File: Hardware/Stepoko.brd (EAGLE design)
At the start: 150 x 80 mm, 172 parts, among them J1 AVR ISP, Q1 16MHZ, Q2 100A/100V, U1 ATMEGA328, U2 CY7C65213, U3 74LVC1G04, U4 LM25011, U5 DRV8811, U6 74HC7014D, U7 74AHC1G08, U8 DRV8811, U9 DRV8811

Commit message: revision changes from review
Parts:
- added C43: 1000pF, SparkFun-Capacitors:0603-CAP
- moved C20 1.02 mm to (15.5, 40.5)
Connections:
- new net N$1: R54.1, U4.7
- net GND: no longer R54.1

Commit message: made changes from design review
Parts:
- removed SJ1: Limit Pull Direction, SparkFun-Passives:PAD-JUMPER-3-2OF3_NC_BY_TRACE_YES_SILK_LARGE
- removed U$3: (no value), SparkFun-Boards:FLANGED_RED_ENCLOSURE-OUTLINE
- added C45, C46: 0.1uF, SparkFun-Capacitors:0603-CAP
- added S5: DPDT, SparkFun-Electromechanical:AYZ0202
- added U$1: (no value), SparkFun-Boards:FLANGED_RED_ENCLOSURE-DIMENSION-NO-INNER-HOLES
- C43: value 1000pF -> 0.1uF
- S1, S2, S3: value 2-POS-DIP -> 2-POS-DIPCTS-THRU-HOLE; device SparkFun-Electromechanical:CHS-02A -> SparkFun-Electromechanical:209-2LPST
- moved S3 1.14 mm to (54.0, 48.0)
- moved C11 1.02 mm to (40.0, 40.5)
- moved C31 1.02 mm to (64.5, 40.5)
- moved S1 0.92 mm to (4.99, 47.8)
- moved S2 0.80 mm to (29.7, 47.8)
- moved LOGO2 0.80 mm to (64.0, 8.89)
- moved D17 0.51 mm to (122.0, 77.3)
- moved R54 0.51 mm to (123.3, 74.6)
- turned C43 to 180 degrees
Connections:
- new net N$4: JP1.1, JP3.1, JP4.1, S5.5
- net 5V: now also S5.1, S5.6; no longer R40.2, SJ1.3
- net ESTOP: now also R40.2; no longer D7.C
- net GND: now also C43.2, C45.2, C46.2, D7.C, S5.3, S5.4; no longer JP1.1, JP3.1, JP4.1, SJ1.1
- net N$95: now also S5.2; no longer SJ1.2
- net VIN: now also C43.1, C45.1, C46.1
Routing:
- net N$4: track 0.00 -> 47.7 mm, vias 0 -> 1
- net 5V: track 521.0 -> 532.5 mm, vias 33 -> 32
- net ESTOP: track 97.2 -> 90.0 mm
- net N$95: track 35.6 -> 42.6 mm
- net N$1: track 0.00 -> 4.19 mm
- net GND: track 0.00 -> 3.39 mm, vias 119 -> 123
- net N$15: track 21.3 -> 20.7 mm, vias 2 -> 1
- net N$34: track 21.3 -> 20.8 mm, vias 2 -> 1
- net N$77: track 22.8 -> 23.3 mm, vias 2 -> 1
- net N$76: track 21.3 -> 21.1 mm, vias 2 -> 1
- net N$35: track 22.8 -> 23.0 mm, vias 2 -> 1
- net N$23: track 22.8 -> 22.9 mm, vias 2 -> 1
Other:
- board text added: "Limit Switch"
- board text added: "Pull Down"
- board text added: "Pull Up"
- board text removed: "Limit"
- board text removed: "Switch Pull +5v-UP GND-DOWN"

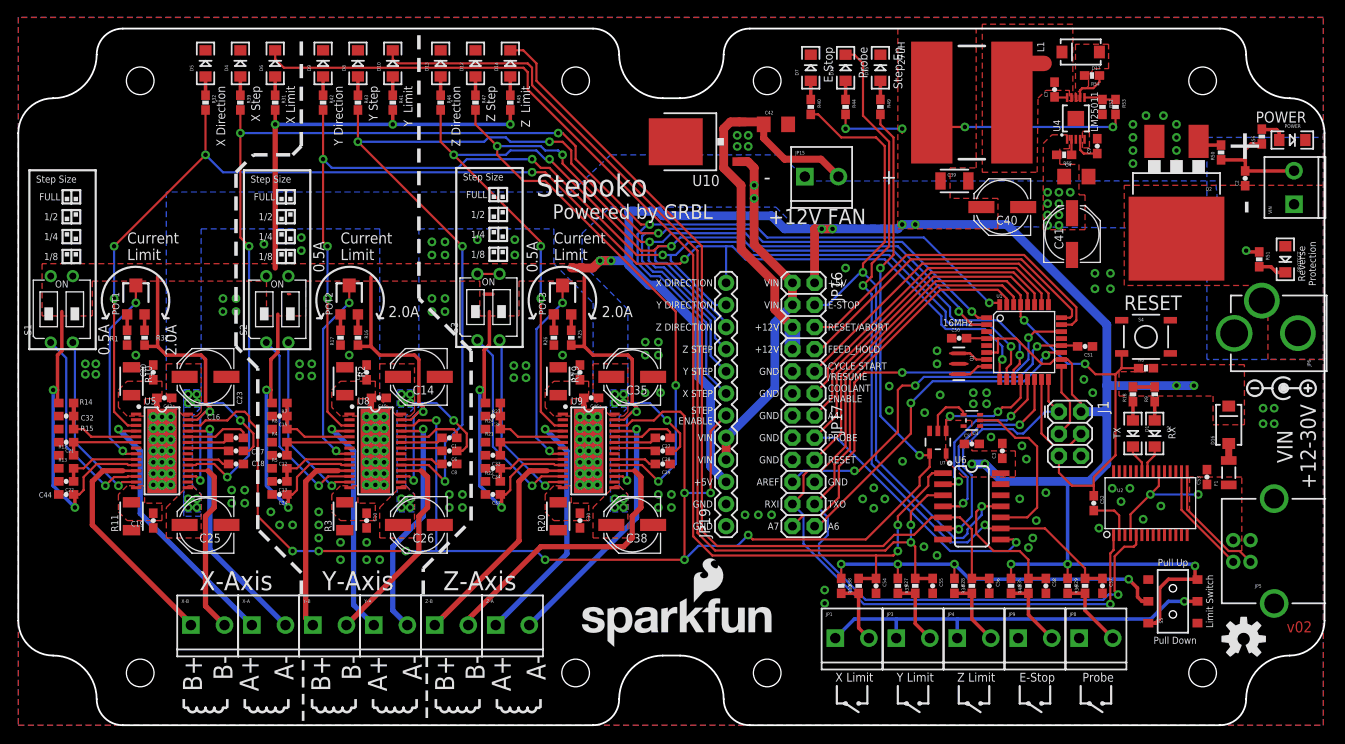
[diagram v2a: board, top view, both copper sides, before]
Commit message: added prod-ids
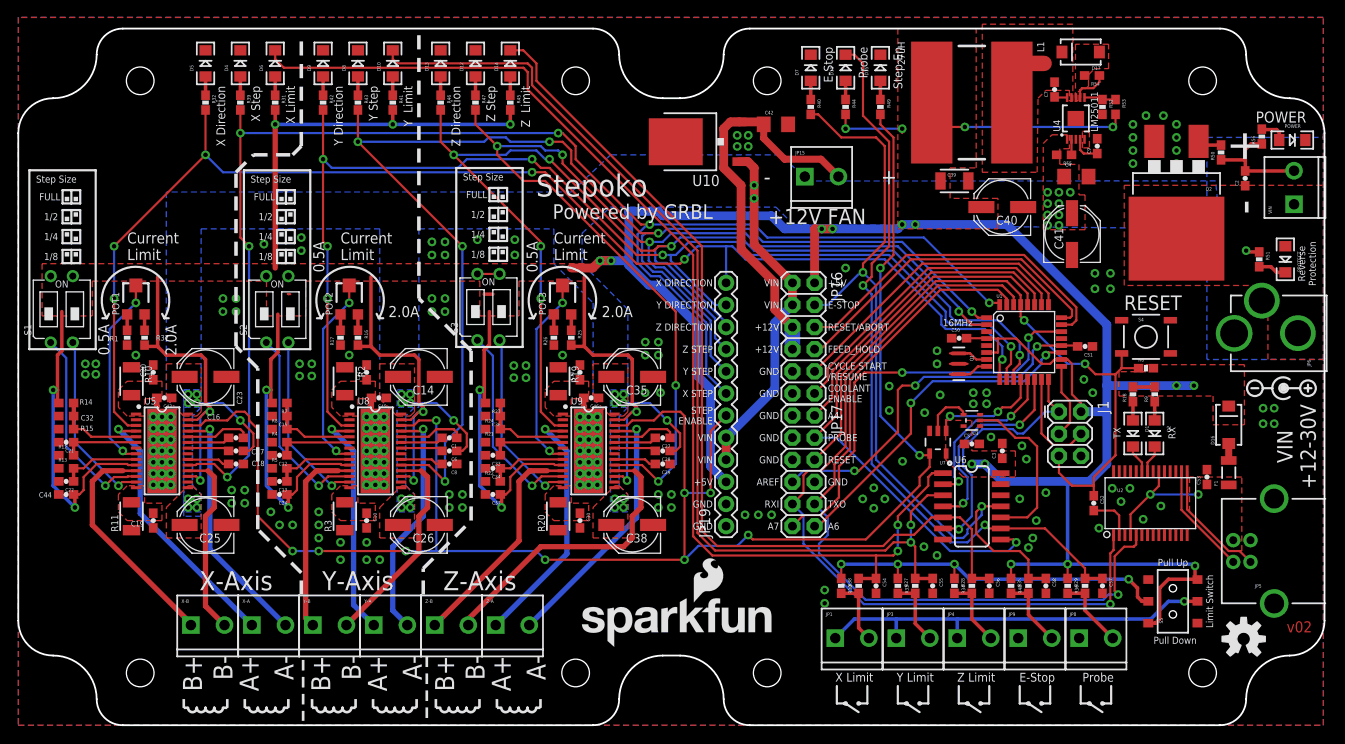
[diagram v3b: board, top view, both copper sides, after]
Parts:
- C15, C32, C36: device SparkFun:0603-CAP -> SparkFun-Capacitors:0603
- R53, R54, R55: device SparkFun-Passives:0603-RES -> SparkFun-Resistors:0603
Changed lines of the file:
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@@
 <attribute name="PROD_ID" value="CAP-10547" x="21.5" y="40" size="1.778" layer="27" rot="R180" display="off"/>
 </element>
-<element name="C32" library="SparkFun" package="0603-CAP" value="0.18uF" x="5.5" y="35.5" smashed="yes" rot="R180">
+<element name="C32" library="SparkFun-Capacitors" package="0603" value="0.18uF" x="5.5" y="35.5" smashed="yes" rot="R180">
 <attribute name="NAME" x="7.1782" y="34.9938" size="0.6096" layer="25" font="vector"/>
 <attribute name="VALUE" x="7.278" y="36.389" size="0.4064" layer="27" font="vector" rot="R270"/>
+<attribute name="PROD_ID" value="CAP-12380" x="5.5" y="35.5" size="1.778" layer="27" rot="R180" display="off"/>
 </element>
 <element name="R37" library="SparkFun-Resistors" package="0603-RES" value="1K" x="14.5" y="44.5" smashed="yes" rot="R270">
@@
 <attribute name="PROD_ID" value="IC-12375" x="16.5" y="31.5" size="1.778" layer="27" rot="R270" display="off"/>
 </element>
-<element name="S1" library="SparkFun-Electromechanical" package="209-2LPST" value="2-POS-DIPCTS-THRU-HOLE" x="4.992" y="47.762"/>
+<element name="S1" library="SparkFun-Electromechanical" package="209-2LPST" value="2-POS-DIPCTS-THRU-HOLE" x="4.992" y="47.762">
+<attribute name="PROD_ID" value="SWCH-12532" x="4.992" y="47.762" size="1.778" layer="27" display="off"/>
+</element>
 <element name="C25" library="SparkFun-Capacitors" package="PANASONIC_D" value="47uF" x="21.5" y="23" rot="R180">
 <attribute name="PROD_ID" value="CAP-10547" x="21.5" y="23" size="1.016" layer="27" font="vector" ratio="15" rot="R180" display="off"/>
@@
 <attribute name="PROD_ID" value="CAP-10547" x="63" y="75" size="1.778" layer="27" rot="R180" display="off"/>
 </element>
-<element name="C15" library="SparkFun" package="0603-CAP" value="0.18uF" x="30" y="35.5" rot="R180"/>
+<element name="C15" library="SparkFun-Capacitors" package="0603" value="0.18uF" x="30" y="35.5" rot="R180">
+<attribute name="PROD_ID" value="CAP-12380" x="30" y="35.5" size="1.778" layer="27" rot="R180" display="off"/>
+</element>
 <element name="R16" library="SparkFun-Resistors" package="0603-RES" value="1K" x="39" y="44.5" rot="R270">
 <attribute name="PROD_ID" value="RES-07856" x="39" y="44.5" size="1.778" layer="27" rot="R270" display="off"/>
@@
 <attribute name="PROD_ID" value="IC-12375" x="41" y="31.5" size="1.778" layer="27" rot="R270" display="off"/>
 </element>
-<element name="S2" library="SparkFun-Electromechanical" package="209-2LPST" value="2-POS-DIPCTS-THRU-HOLE" x="29.746" y="47.762"/>
+<element name="S2" library="SparkFun-Electromechanical" package="209-2LPST" value="2-POS-DIPCTS-THRU-HOLE" x="29.746" y="47.762">
+<attribute name="PROD_ID" value="SWCH-12532" x="29.746" y="47.762" size="1.778" layer="27" display="off"/>
+</element>
 <element name="C26" library="SparkFun-Capacitors" package="PANASONIC_D" value="47uF" x="46" y="23" rot="R180">
 <attribute name="PROD_ID" value="CAP-10547" x="53.5" y="100.5" size="1.778" layer="27" rot="R180" display="off"/>
@@
 <attribute name="PROD_ID" value="CAP-10547" x="87.5" y="75" size="1.778" layer="27" rot="R180" display="off"/>
 </element>
-<element name="C36" library="SparkFun" package="0603-CAP" value="0.18uF" x="54.5" y="35.5" rot="R180"/>
+<element name="C36" library="SparkFun-Capacitors" package="0603" value="0.18uF" x="54.5" y="35.5" rot="R180">
+<attribute name="PROD_ID" value="CAP-12380" x="54.5" y="35.5" size="1.778" layer="27" rot="R180" display="off"/>
+</element>
 <element name="R25" library="SparkFun-Resistors" package="0603-RES" value="1K" x="63.5" y="44.5" rot="R270">
 <attribute name="PROD_ID" value="RES-07856" x="63.5" y="44.5" size="1.778" layer="27" rot="R270" display="off"/>
@@
 <attribute name="PROD_ID" value="IC-12375" x="65.5" y="31.5" size="1.778" layer="27" rot="R270" display="off"/>
 </element>
-<element name="S3" library="SparkFun-Electromechanical" package="209-2LPST" value="2-POS-DIPCTS-THRU-HOLE" x="53.992" y="48.016"/>
+<element name="S3" library="SparkFun-Electromechanical" package="209-2LPST" value="2-POS-DIPCTS-THRU-HOLE" x="53.992" y="48.016">
+<attribute name="PROD_ID" value="SWCH-12532" x="53.992" y="48.016" size="1.778" layer="27" display="off"/>
+</element>
 <element name="C38" library="SparkFun-Capacitors" package="PANASONIC_D" value="47uF" x="70.5" y="23" rot="R180">
 <attribute name="PROD_ID" value="CAP-10547" x="78" y="100.5" size="1.778" layer="27" rot="R180" display="off"/>
@@
 <attribute name="VALUE" value="MBRA140" x="122" y="77.308" size="1.778" layer="27" rot="R180" display="off"/>
 </element>
-<element name="R53" library="SparkFun-Passives" package="0603-RES" value="9.76K" x="126" y="71" rot="R270"/>
-<element name="R54" library="SparkFun-Passives" package="0603-RES" value="50.0m" x="123.3" y="74.608" rot="R180"/>
-<element name="R55" library="SparkFun-Passives" package="0603-RES" value="348K" x="120.1" y="65.5" rot="R180"/>
+<element name="R53" library="SparkFun-Resistors" package="0603" value="9.76K" x="126" y="71" rot="R270">
+<attribute name="PROD_ID" value="RES-12534" x="126" y="71" size="1.778" layer="27" rot="R270" display="off"/>
+</element>
+<element name="R54" library="SparkFun-Resistors" package="0603" value="50.0m" x="123.3" y="74.608" rot="R180">
+<attribute name="PROD_ID" value="RES-12535" x="123.3" y="74.608" size="1.778" layer="27" rot="R180" display="off"/>
+</element>
+<element name="R55" library="SparkFun-Resistors" package="0603" value="348K" x="120.1" y="65.5" rot="R180">
+<attribute name="PROD_ID" value="RES-12533" x="120.1" y="65.5" size="1.778" layer="27" rot="R180" display="off"/>
+</element>
 <element name="L1" library="SparkFun-Passives" package="INDUCTOR_SDR1307" value="27uH" x="109.5" y="71.5" rot="R270">
 <attribute name="PROD_ID" value="NDUC-12529" x="109.5" y="71.5" size="1.016" layer="27" font="vector" ratio="15" rot="R270" display="off"/>
